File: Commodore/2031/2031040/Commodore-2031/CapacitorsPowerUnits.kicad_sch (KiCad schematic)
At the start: 47 parts

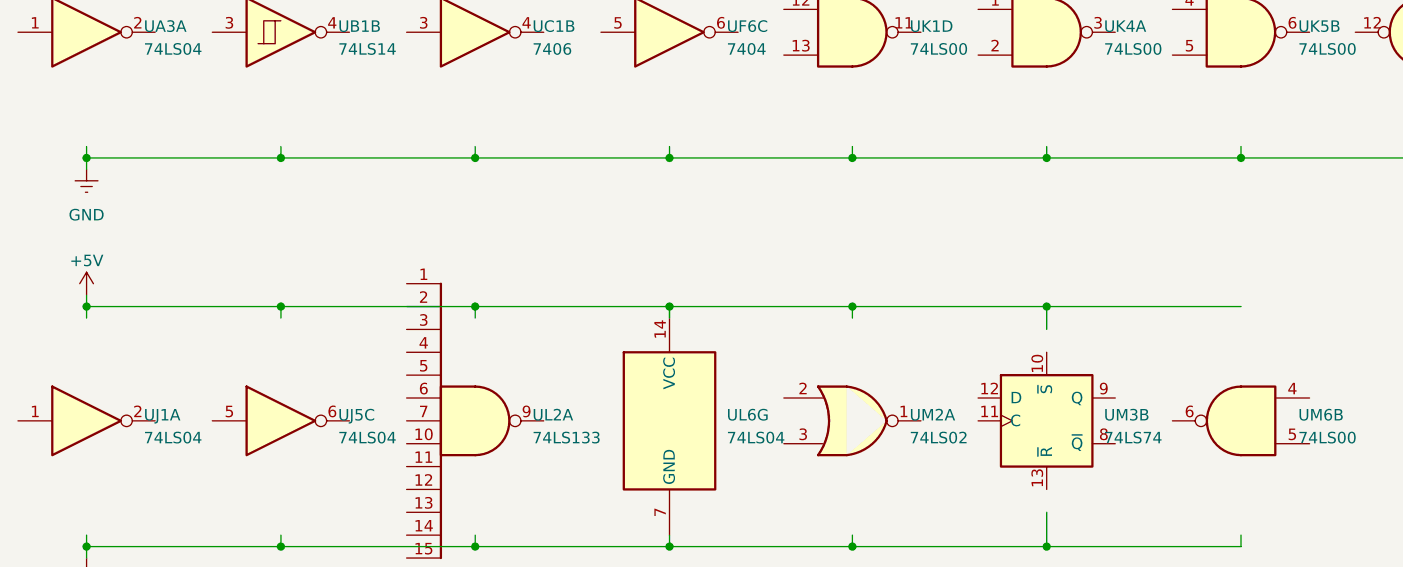
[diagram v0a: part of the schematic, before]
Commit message: Resolve remaining ERC errors
... still lots of warnings tho.
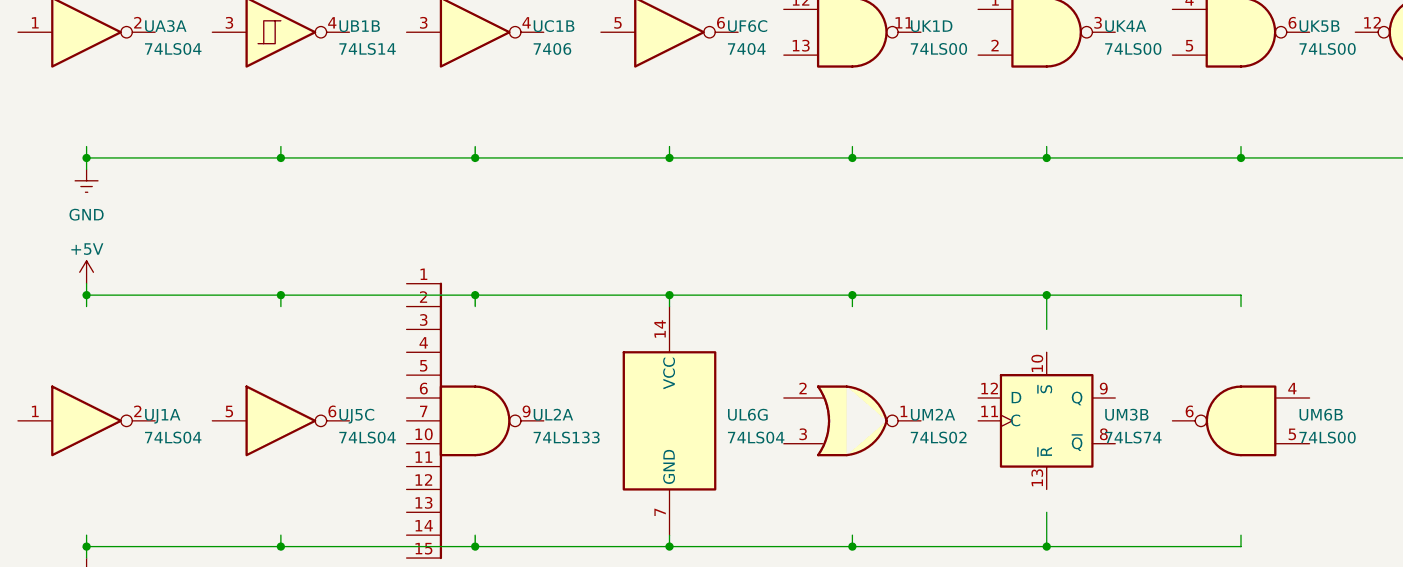
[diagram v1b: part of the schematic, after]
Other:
- title: (none) -> Capacitors & Power Units
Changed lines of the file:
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@@
 (kicad_sch (version 20230121) (generator eeschema)
   (paper "A4")
-  (junction (at 29.21 111.76) (diameter 0) (color 0 0 0 0)
+  (title_block
+    (title "Capacitors & Power Units")
+    (comment 1 "Schematic 203138")
+    (comment 2 "PCB Assembly 2031040")
+    (comment 4 "captured from original service manual by @rjhelms")
+  )
+  (junction (at 29.21 110.49) (diameter 0) (color 0 0 0 0)
   )
   (junction (at 95.25 54.61) (diameter 0) (color 0 0 0 0)
@@
   (junction (at 68.58 46.99) (diameter 0) (color 0 0 0 0)
   )
-  (junction (at 114.3 111.76) (diameter 0) (color 0 0 0 0)
+  (junction (at 114.3 110.49) (diameter 0) (color 0 0 0 0)
   )
   (junction (at 121.92 54.61) (diameter 0) (color 0 0 0 0)
@@
   (junction (at 113.03 24.13) (diameter 0) (color 0 0 0 0)
   )
-  (junction (at 135.89 111.76) (diameter 0) (color 0 0 0 0)
+  (junction (at 135.89 110.49) (diameter 0) (color 0 0 0 0)
   )
   (junction (at 59.69 54.61) (diameter 0) (color 0 0 0 0)
@@
   (junction (at 68.58 54.61) (diameter 0) (color 0 0 0 0)
   )
-  (junction (at 72.39 111.76) (diameter 0) (color 0 0 0 0)
-  )
-  (junction (at 50.8 111.76) (diameter 0) (color 0 0 0 0)
+  (junction (at 72.39 110.49) (diameter 0) (color 0 0 0 0)
+  )
+  (junction (at 50.8 110.49) (diameter 0) (color 0 0 0 0)
   )
   (junction (at 50.8 181.61) (diameter 0) (color 0 0 0 0)
@@
   (junction (at 77.47 54.61) (diameter 0) (color 0 0 0 0)
   )
-  (junction (at 93.98 111.76) (diameter 0) (color 0 0 0 0)
+  (junction (at 93.98 110.49) (diameter 0) (color 0 0 0 0)
   )
   (junction (at 68.58 31.75) (diameter 0) (color 0 0 0 0)
@@
     (stroke (width 0) (type default))
   )
-  (wire (pts (xy 135.89 111.76) (xy 157.48 111.76))
+  (wire (pts (xy 135.89 110.49) (xy 157.48 110.49))
     (stroke (width 0) (type default))
   )
@@
     (stroke (width 0) (type default))
   )
-  (wire (pts (xy 135.89 111.76) (xy 135.89 114.3))
+  (wire (pts (xy 135.89 110.49) (xy 135.89 114.3))
     (stroke (width 0) (type default))
   )
@@
     (stroke (width 0) (type default))
   )
+  (wire (pts (xy 93.98 110.49) (xy 93.98 111.76))
+    (stroke (width 0) (type default))
+  )
   (wire (pts (xy 68.58 54.61) (xy 77.47 54.61))
     (stroke (width 0) (type default))
@@
     (stroke (width 0) (type default))
   )
-  (wire (pts (xy 29.21 111.76) (xy 50.8 111.76))
+  (wire (pts (xy 29.21 110.49) (xy 50.8 110.49))
     (stroke (width 0) (type default))
   )
@@
     (stroke (width 0) (type default))
   )
-  (wire (pts (xy 72.39 111.76) (xy 72.39 113.03))
-    (stroke (width 0) (type default))
-  )
   (wire (pts (xy 135.89 93.98) (xy 135.89 95.25))
     (stroke (width 0) (type default))
@@
     (stroke (width 0) (type default))
   )
-  (wire (pts (xy 114.3 111.76) (xy 114.3 113.03))
-    (stroke (width 0) (type default))
-  )
   (wire (pts (xy 50.8 24.13) (xy 59.69 24.13))
     (stroke (width 0) (type default))
   )
+  (wire (pts (xy 72.39 110.49) (xy 72.39 111.76))
+    (stroke (width 0) (type default))
+  )
   (wire (pts (xy 157.48 31.75) (xy 157.48 30.48))
     (stroke (width 0) (type default))
@@
     (stroke (width 0) (type default))
   )
-  (wire (pts (xy 29.21 113.03) (xy 29.21 111.76))
-    (stroke (width 0) (type default))
-  )
   (wire (pts (xy 157.48 93.98) (xy 157.48 95.25))
     (stroke (width 0) (type default))
@@
     (stroke (width 0) (type default))
   )
-  (wire (pts (xy 72.39 111.76) (xy 93.98 111.76))
+  (wire (pts (xy 72.39 110.49) (xy 93.98 110.49))
     (stroke (width 0) (type default))
   )
@@
     (stroke (width 0) (type default))
   )
-  (wire (pts (xy 50.8 111.76) (xy 72.39 111.76))
+  (wire (pts (xy 50.8 110.49) (xy 72.39 110.49))
     (stroke (width 0) (type default))
   )
@@
     (stroke (width 0) (type default))
   )
-  (wire (pts (xy 93.98 111.76) (xy 93.98 113.03))
-    (stroke (width 0) (type default))
-  )
   (wire (pts (xy 93.98 180.34) (xy 93.98 181.61))
     (stroke (width 0) (type default))
@@
     (stroke (width 0) (type default))
   )
-  (wire (pts (xy 114.3 111.76) (xy 135.89 111.76))
+  (wire (pts (xy 114.3 110.49) (xy 135.89 110.49))
     (stroke (width 0) (type default))
   )
@@
     (stroke (width 0) (type default))
   )
+  (wire (pts (xy 29.21 110.49) (xy 29.21 111.76))
+    (stroke (width 0) (type default))
+  )
   (wire (pts (xy 177.8 93.98) (xy 177.8 95.25))
     (stroke (width 0) (type default))
@@
     (stroke (width 0) (type default))
   )
-  (wire (pts (xy 29.21 110.49) (xy 29.21 111.76))
+  (wire (pts (xy 29.21 109.22) (xy 29.21 110.49))
     (stroke (width 0) (type default))
   )
@@
     (stroke (width 0) (type default))
   )
+  (wire (pts (xy 50.8 110.49) (xy 50.8 111.76))
+    (stroke (width 0) (type default))
+  )
   (wire (pts (xy 29.21 181.61) (xy 29.21 182.88))
     (stroke (width 0) (type default))
@@
     (stroke (width 0) (type default))
   )
-  (wire (pts (xy 50.8 111.76) (xy 50.8 113.03))
-    (stroke (width 0) (type default))
-  )
   (wire (pts (xy 121.92 46.99) (xy 121.92 48.26))
     (stroke (width 0) (type default))
   )
+  (wire (pts (xy 157.48 110.49) (xy 157.48 111.76))
+    (stroke (width 0) (type default))
+  )
   (wire (pts (xy 95.25 46.99) (xy 104.14 46.99))
     (stroke (width 0) (type default))
@@
     (stroke (width 0) (type default))
   )
+  (wire (pts (xy 114.3 110.49) (xy 114.3 111.76))
+    (stroke (width 0) (type default))
+  )
   (wire (pts (xy 95.25 46.99) (xy 95.25 48.26))
     (stroke (width 0) (type default))
@@
     (stroke (width 0) (type default))
   )
-  (wire (pts (xy 93.98 111.76) (xy 114.3 111.76))
+  (wire (pts (xy 93.98 110.49) (xy 114.3 110.49))
     (stroke (width 0) (type default))
   )
@@
     )
   )
-  (symbol (lib_id "power:+5V") (at 29.21 110.49 0) (unit 1)
+  (symbol (lib_id "power:+5V") (at 29.21 109.22 0) (unit 1)
     (in_bom yes) (on_board yes) (dnp no) (fields_autoplaced)
-    (property "Reference" "#PWR0112" (at 29.21 114.3 0)
-      (effects (font (size 1.27 1.27)) hide)
-    )
-    (property "Value" "+5V" (at 29.21 106.68 0)
+    (property "Reference" "#PWR0112" (at 29.21 113.03 0)
+      (effects (font (size 1.27 1.27)) hide)
+    )
+    (property "Value" "+5V" (at 29.21 105.41 0)
       (effects (font (size 1.27 1.27)))
     )
-    (property "Footprint" "" (at 29.21 110.49 0)
-      (effects (font (size 1.27 1.27)) hide)
-    )
-    (property "Datasheet" "" (at 29.21 110.49 0)
-      (effects (font (size 1.27 1.27)) hide)
-    )
+    (property "Footprint" "" (at 29.21 109.22 0)
+      (effects (font (size 1.27 1.27)) hide)
+    )
+    (property "Datasheet" "" (at 29.21 109.22 0)
+      (effects (font (size 1.27 1.27)) hide)
+    )
